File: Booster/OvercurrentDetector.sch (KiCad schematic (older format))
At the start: 37 parts, among them U203 LM339, U501 LM338, U502 LM358, U503 NE555, U504 74HC08

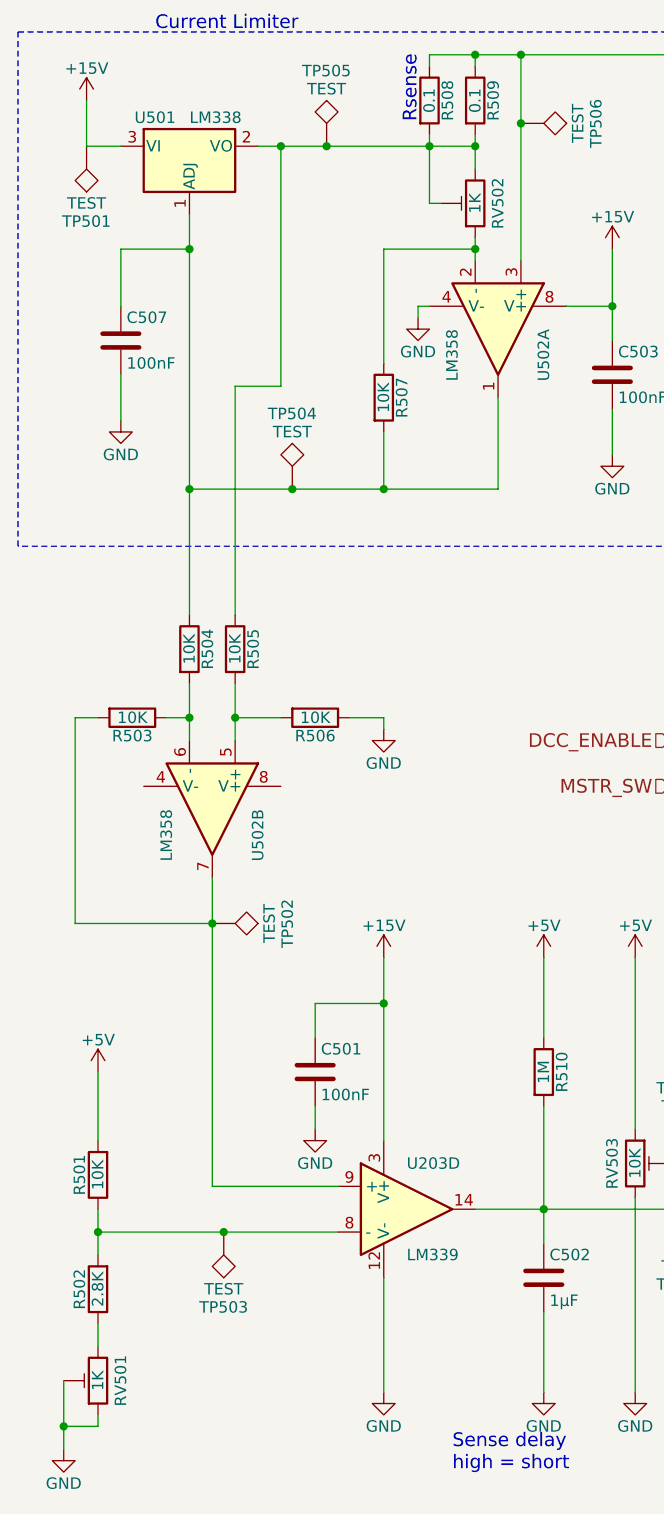
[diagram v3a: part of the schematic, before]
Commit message: Starting to add traces. Minor schematic changes to aid routing.
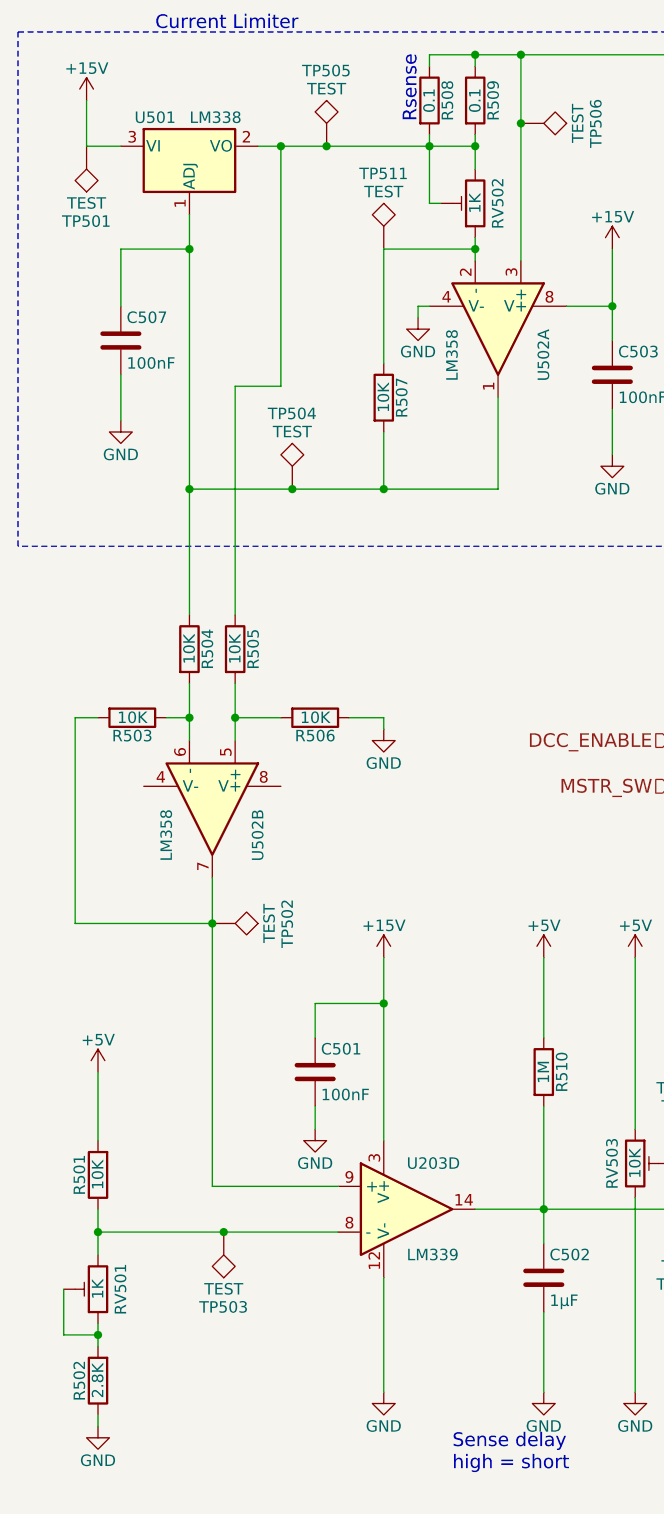
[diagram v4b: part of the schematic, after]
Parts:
- added TP511: TEST, Measurement_Points:Measurement_Point_Round-TH_Small, symbol TEST
- R508, R509: footprint Resistors_SMD:R_0805 -> Resistors_THT:R_Axial_DIN0207_L6.3mm_D2.5mm_P7.62mm_Horizontal
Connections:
- net GND: now also R502.1; no longer RV501.1, RV501.2
- net at RV501.3: now also R501.1, TP503.1, U203.8 (-); no longer R502.1
- net at R507.1, RV502.1, U502.2 (-): now also TP511.1
- new net: R502.2, RV501.1, RV501.2
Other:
- moved on the sheet: R502, RV501
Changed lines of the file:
@@
 L R R502
 U 1 1 59ECC864
-P 2650 6400
-F 0 "R502" V 2730 6400 50  0000 C CNN
-F 1 "2.8K" V 2650 6400 50  0000 C CNN
-F 2 "Resistors_SMD:R_0805" V 2580 6400 50  0001 C CNN
-F 3 "" H 2650 6400 50  0000 C CNN
-	1    2650 6400
+P 2650 6800
+F 0 "R502" V 2730 6800 50  0000 C CNN
+F 1 "2.8K" V 2650 6800 50  0000 C CNN
+F 2 "Resistors_SMD:R_0805" V 2580 6800 50  0001 C CNN
+F 3 "" H 2650 6800 50  0000 C CNN
+	1    2650 6800
 	-1   0    0    1
 $EndComp
@@
 $EndComp
 $Comp
-L GND #PWR019
+L GND #PWR503
 U 1 1 59ECCA64
-P 2500 7100
-F 0 "#PWR019" H 2500 6850 50  0001 C CNN
-F 1 "GND" H 2500 6950 50  0000 C CNN
-F 2 "" H 2500 7100 50  0000 C CNN
-F 3 "" H 2500 7100 50  0000 C CNN
-	1    2500 7100
+P 2650 7000
+F 0 "#PWR503" H 2650 6750 50  0001 C CNN
+F 1 "GND" H 2650 6850 50  0000 C CNN
+F 2 "" H 2650 7000 50  0000 C CNN
+F 3 "" H 2650 7000 50  0000 C CNN
+	1    2650 7000
 	1    0    0    -1
 $EndComp
@@
 F 0 "R509" V 4380 1200 50  0000 C CNN
 F 1 "0.1" V 4300 1200 50  0000 C CNN
-F 2 "Resistors_SMD:R_0805" V 4230 1200 50  0001 C CNN
+F 2 "Resistors_THT:R_Axial_DIN0207_L6.3mm_D2.5mm_P7.62mm_Horizontal" V 4230 1200 50  0001 C CNN
 F 3 "" H 4300 1200 50  0001 C CNN
 	1    4300 1200
@@
 F 0 "R508" V 4180 1200 50  0000 C CNN
 F 1 "0.1" V 4100 1200 50  0000 C CNN
-F 2 "Resistors_SMD:R_0805" V 4030 1200 50  0001 C CNN
+F 2 "Resistors_THT:R_Axial_DIN0207_L6.3mm_D2.5mm_P7.62mm_Horizontal" V 4030 1200 50  0001 C CNN
 F 3 "" H 4100 1200 50  0001 C CNN
 	1    4100 1200
@@
 $EndComp
 $Comp
-L GND #PWR020
+L GND #PWR509
 U 1 1 5A073D4C
 P 4050 2150
-F 0 "#PWR020" H 4050 1900 50  0001 C CNN
+F 0 "#PWR509" H 4050 1900 50  0001 C CNN
 F 1 "GND" H 4050 2000 50  0000 C CNN
 F 2 "" H 4050 2150 50  0000 C CNN
@@
 $EndComp
 $Comp
-L GND #PWR021
+L GND #PWR513
 U 1 1 5A074775
 P 4900 2750
-F 0 "#PWR021" H 4900 2500 50  0001 C CNN
+F 0 "#PWR513" H 4900 2500 50  0001 C CNN
 F 1 "GND" H 4900 2600 50  0000 C CNN
 F 2 "" H 4900 2750 50  0000 C CNN
@@
 $EndComp
 $Comp
-L GND #PWR022
+L GND #PWR506
 U 1 1 5A076EC5
 P 3900 3950
-F 0 "#PWR022" H 3900 3700 50  0001 C CNN
+F 0 "#PWR506" H 3900 3700 50  0001 C CNN
 F 1 "GND" H 3900 3800 50  0000 C CNN
 F 2 "" H 3900 3950 50  0000 C CNN
@@
 $EndComp
 $Comp
-L +5V #PWR023
+L +5V #PWR502
 U 1 1 5A081F18
 P 2650 5450
-F 0 "#PWR023" H 2650 5300 50  0001 C CNN
+F 0 "#PWR502" H 2650 5300 50  0001 C CNN
 F 1 "+5V" H 2650 5590 50  0000 C CNN
 F 2 "" H 2650 5450 50  0000 C CNN
@@
 L POT_TRIM RV501
 U 1 1 5A082A09
-P 2650 6800
-F 0 "RV501" V 2550 6800 50  0000 C CNN
-F 1 "1K" V 2650 6800 50  0000 C CNN
-F 2 "Potentiometers:Potentiometer_Trimmer_Bourns_3296W" H 2650 6800 50  0001 C CNN
-F 3 "" H 2650 6800 50  0001 C CNN
-	1    2650 6800
+P 2650 6400
+F 0 "RV501" V 2550 6400 50  0000 C CNN
+F 1 "1K" V 2650 6400 50  0000 C CNN
+F 2 "Potentiometers:Potentiometer_Trimmer_Bourns_3296W" H 2650 6400 50  0001 C CNN
+F 3 "" H 2650 6400 50  0001 C CNN
+	1    2650 6400
 	-1   0    0    1
 $EndComp
@@
 $EndComp
 $Comp
-L GND #PWR024
+L GND #PWR505
 U 1 1 5A092416
 P 3600 5700
-F 0 "#PWR024" H 3600 5450 50  0001 C CNN
+F 0 "#PWR505" H 3600 5450 50  0001 C CNN
 F 1 "GND" H 3600 5550 50  0000 C CNN
 F 2 "" H 3600 5700 50  0000 C CNN
@@
 $EndComp
 $Comp
-L +5V #PWR025
+L +5V #PWR510
 U 1 1 5A092870
 P 4600 4950
-F 0 "#PWR025" H 4600 4800 50  0001 C CNN
+F 0 "#PWR510" H 4600 4800 50  0001 C CNN
 F 1 "+5V" H 4600 5090 50  0000 C CNN
 F 2 "" H 4600 4950 50  0000 C CNN
@@
 $EndComp
 $Comp
-L +5V #PWR026
+L +5V #PWR514
 U 1 1 5A092928
 P 5000 4950
-F 0 "#PWR026" H 5000 4800 50  0001 C CNN
+F 0 "#PWR514" H 5000 4800 50  0001 C CNN
 F 1 "+5V" H 5000 5090 50  0000 C CNN
 F 2 "" H 5000 4950 50  0000 C CNN
@@
 $EndComp
 $Comp
-L GND #PWR027
+L GND #PWR508
 U 1 1 5A0931C8
 P 3900 6850
-F 0 "#PWR027" H 3900 6600 50  0001 C CNN
+F 0 "#PWR508" H 3900 6600 50  0001 C CNN
 F 1 "GND" H 3900 6700 50  0000 C CNN
 F 2 "" H 3900 6850 50  0000 C CNN
@@
 $EndComp
 $Comp
-L GND #PWR028
+L GND #PWR511
 U 1 1 5A093221
 P 4600 6850
-F 0 "#PWR028" H 4600 6600 50  0001 C CNN
+F 0 "#PWR511" H 4600 6600 50  0001 C CNN
 F 1 "GND" H 4600 6700 50  0000 C CNN
 F 2 "" H 4600 6850 50  0000 C CNN
@@
 $EndComp
 $Comp
-L GND #PWR029
+L GND #PWR515
 U 1 1 5A09327A
 P 5000 6850
-F 0 "#PWR029" H 5000 6600 50  0001 C CNN
+F 0 "#PWR515" H 5000 6600 50  0001 C CNN
 F 1 "GND" H 5000 6700 50  0000 C CNN
 F 2 "" H 5000 6850 50  0000 C CNN
@@
 $EndComp
 $Comp
-L +15V #PWR030
+L +15V #PWR501
 U 1 1 5A093E23
 P 2600 1200
-F 0 "#PWR030" H 2600 1050 50  0001 C CNN
+F 0 "#PWR501" H 2600 1050 50  0001 C CNN
 F 1 "+15V" H 2600 1340 50  0000 C CNN
 F 2 "" H 2600 1200 50  0000 C CNN
@@
 $EndComp
 $Comp
-L +15V #PWR031
+L +15V #PWR507
 U 1 1 5A094178
 P 3900 4950
-F 0 "#PWR031" H 3900 4800 50  0001 C CNN
+F 0 "#PWR507" H 3900 4800 50  0001 C CNN
 F 1 "+15V" H 3900 5090 50  0000 C CNN
 F 2 "" H 3900 4950 50  0000 C CNN
@@
 $EndComp
 $Comp
-L +15V #PWR032
+L +15V #PWR512
 U 1 1 5A0943E3
 P 4900 1850
-F 0 "#PWR032" H 4900 1700 50  0001 C CNN
+F 0 "#PWR512" H 4900 1700 50  0001 C CNN
 F 1 "+15V" H 4900 1990 50  0000 C CNN
 F 2 "" H 4900 1850 50  0000 C CNN
@@
 $EndComp
 $Comp
-L +5V #PWR033
+L +5V #PWR516
 U 1 1 5A36B721
 P 5950 4950
-F 0 "#PWR033" H 5950 4800 50  0001 C CNN
+F 0 "#PWR516" H 5950 4800 50  0001 C CNN
 F 1 "+5V" H 5950 5090 50  0000 C CNN
 F 2 "" H 5950 4950 50  0000 C CNN
@@
 $EndComp
 $Comp
-L +5V #PWR034
+L +5V #PWR518
 U 1 1 5A36C438
 P 8550 3850
-F 0 "#PWR034" H 8550 3700 50  0001 C CNN
+F 0 "#PWR518" H 8550 3700 50  0001 C CNN
 F 1 "+5V" H 8550 3990 50  0000 C CNN
 F 2 "" H 8550 3850 50  0000 C CNN
@@
 $EndComp
 $Comp
-L GND #PWR035
+L GND #PWR519
 U 1 1 5A36CF5F
 P 8550 4500
-F 0 "#PWR035" H 8550 4250 50  0001 C CNN
+F 0 "#PWR519" H 8550 4250 50  0001 C CNN
 F 1 "GND" H 8550 4350 50  0000 C CNN
 F 2 "" H 8550 4500 50  0000 C CNN
@@
 $EndComp
 $Comp
-L +5V #PWR036
+L +5V #PWR520
 U 1 1 5A36D304
 P 9000 3850
-F 0 "#PWR036" H 9000 3700 50  0001 C CNN
+F 0 "#PWR520" H 9000 3700 50  0001 C CNN
 F 1 "+5V" H 9000 3990 50  0000 C CNN
 F 2 "" H 9000 3850 50  0000 C CNN
@@
 	3900 2900 3900 2650
 Connection ~ 3900 2900
-Wire Wire Line
-	4300 1850 3900 1850
-Wire Wire Line
-	3900 1850 3900 2350
 Connection ~ 4300 1850
 Wire Wire Line
@@
 Wire Wire Line
 	2650 6950 2650 7000
-Wire Wire Line
-	2650 7000 2500 7000
-Connection ~ 2500 7000
 Wire Notes Line
 	2300 900  5200 900
@@
 Connection ~ 8250 6000
 $Comp
-L GND #PWR037
+L GND #PWR517
 U 1 1 5A36DC1B
 P 8250 6150
-F 0 "#PWR037" H 8250 5900 50  0001 C CNN
+F 0 "#PWR517" H 8250 5900 50  0001 C CNN
 F 1 "GND" H 8250 6000 50  0000 C CNN
 F 2 "" H 8250 6150 50  0000 C CNN
@@
 Wire Wire Line
 	5150 4000 6050 4000
-Wire Wire Line
-	2500 6800 2500 7100
 Connection ~ 3050 1850
 Wire Wire Line
@@
 	2750 2400 2750 2600
 $Comp
-L GND #PWR038
+L GND #PWR504
 U 1 1 5A413136
 P 2750 2600
-F 0 "#PWR038" H 2750 2350 50  0001 C CNN
+F 0 "#PWR504" H 2750 2350 50  0001 C CNN
 F 1 "GND" H 2750 2450 50  0000 C CNN
 F 2 "" H 2750 2600 50  0000 C CNN
@@
 	1    0    0    -1
 $EndComp
+Wire Wire Line
+	2650 6600 2500 6600
+Wire Wire Line
+	2500 6600 2500 6400
+Connection ~ 2650 6600
+$Comp
+L TEST TP511
+U 1 1 5A458E86
+P 3900 1850
+F 0 "TP511" H 3900 2150 50  0000 C BNN
+F 1 "TEST" H 3900 2100 50  0000 C CNN
+F 2 "Measurement_Points:Measurement_Point_Round-TH_Small" H 3900 1850 50  0001 C CNN
+F 3 "" H 3900 1850 50  0001 C CNN
+	1    3900 1850
+	1    0    0    -1
+$EndComp
+Wire Wire Line
+	3900 2350 3900 1850
+Wire Wire Line
+	3900 1850 4300 1850
 $EndSCHEMATC
